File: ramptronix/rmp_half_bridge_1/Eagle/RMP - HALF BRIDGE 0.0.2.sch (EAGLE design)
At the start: 66 parts

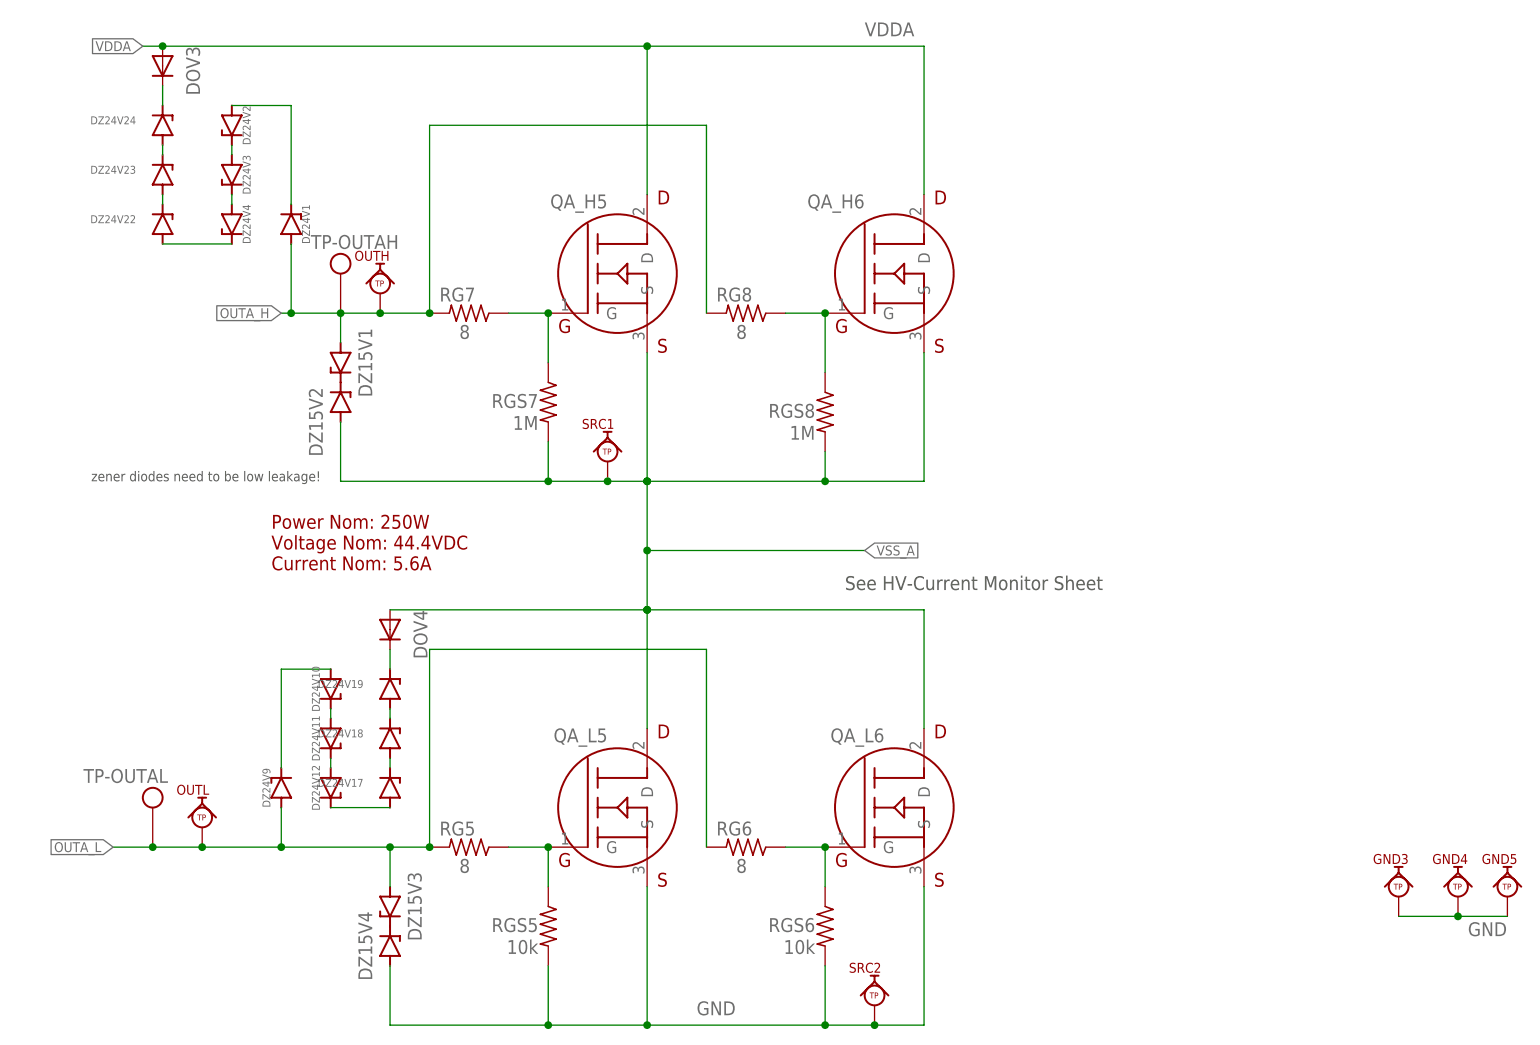
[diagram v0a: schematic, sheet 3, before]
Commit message: Half Bridge - 0.0.2
Half Bridge - 0.0.2
Fixed net issue with OV clamp/crowbar
Increased voltage rating of MOSFETs
Increased voltage rating of CAPS
Increased clearances for 400V operation
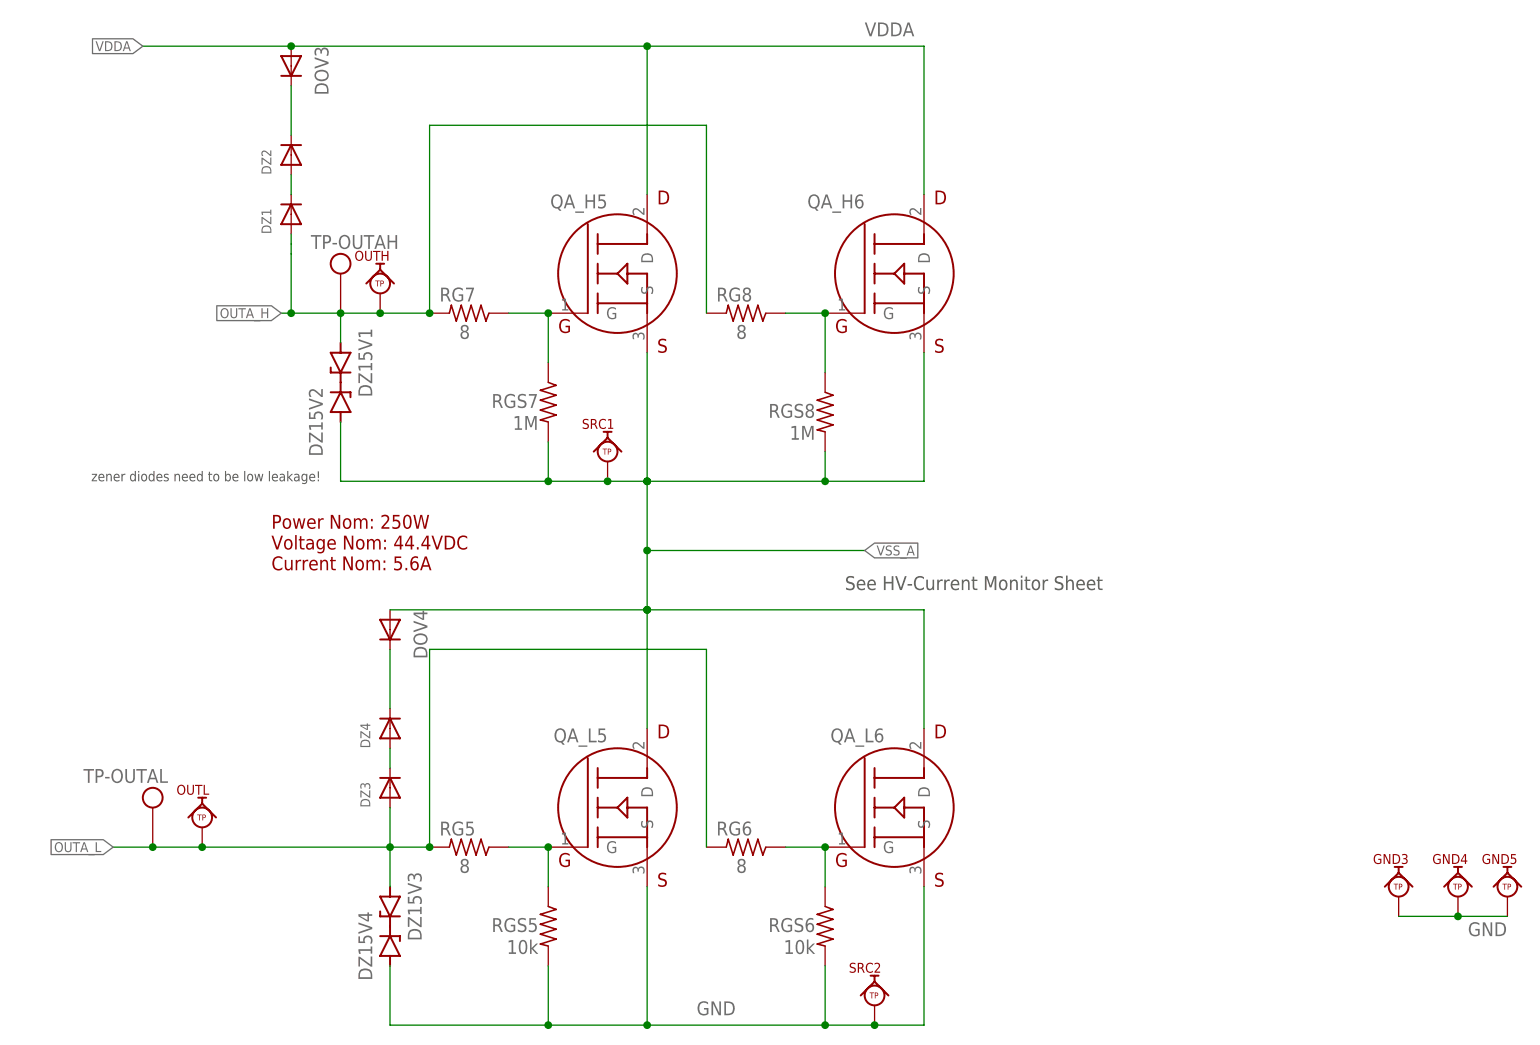
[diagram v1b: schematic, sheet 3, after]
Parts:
- removed DZ24V1, DZ24V10, DZ24V11, DZ24V12, DZ24V17, DZ24V18, DZ24V19, DZ24V2, DZ24V22, DZ24V23, DZ24V24, DZ24V3, DZ24V4, DZ24V9: NZH15B,115, Diode:ZENER_MMSZ5240BTDO-219-AB(SOD123F)
- added DZ1, DZ2, DZ3, DZ4: (no value), adafruit:DIODESMA
- CHV1, CHV2, CVH3, CVH4: LCSC_PART C342270 -> DNP/C342270
- QA_H5, QA_H6, QA_L5, QA_L6: LCSC_PART DNP -> C604524
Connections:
- removed net N$25: DZ24V10.C, DZ24V11.A
- removed net N$26: DZ24V11.C, DZ24V12.A
- removed net N$33: DZ24V10.A, DZ24V9.C
- removed net N$34: DZ24V17.C, DZ24V18.A
- removed net N$35: DZ24V18.C, DZ24V19.A
- removed net N$36: DOV4.C, DZ24V19.C
- removed net N$4: DZ24V22.A, DZ24V4.C
- removed net N$40: DZ24V22.C, DZ24V23.A
- removed net N$42: DZ24V23.C, DZ24V24.A
- removed net N$5: DZ24V12.C, DZ24V17.A
- net N$1: now also DZ1.C, DZ2.A; no longer DZ24V2.C, DZ24V3.A
- net N$2: now also DOV4.C, DZ4.C; no longer DZ24V3.C, DZ24V4.A
- net N$3: now also DZ3.C, DZ4.A; no longer DZ24V1.C, DZ24V2.A
- net N$47: now also DZ2.C; no longer DZ24V24.C
- net OUTA_H: now also DZ1.A; no longer DZ24V1.A
- net OUTA_L: now also DZ3.A; no longer DZ24V9.A
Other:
- moved on the sheet: DOV3
